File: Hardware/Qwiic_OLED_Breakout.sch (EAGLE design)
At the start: 30 parts, among them J1 QWIIC_RIGHT_ANGLE, J2 QWIIC_RIGHT_ANGLE

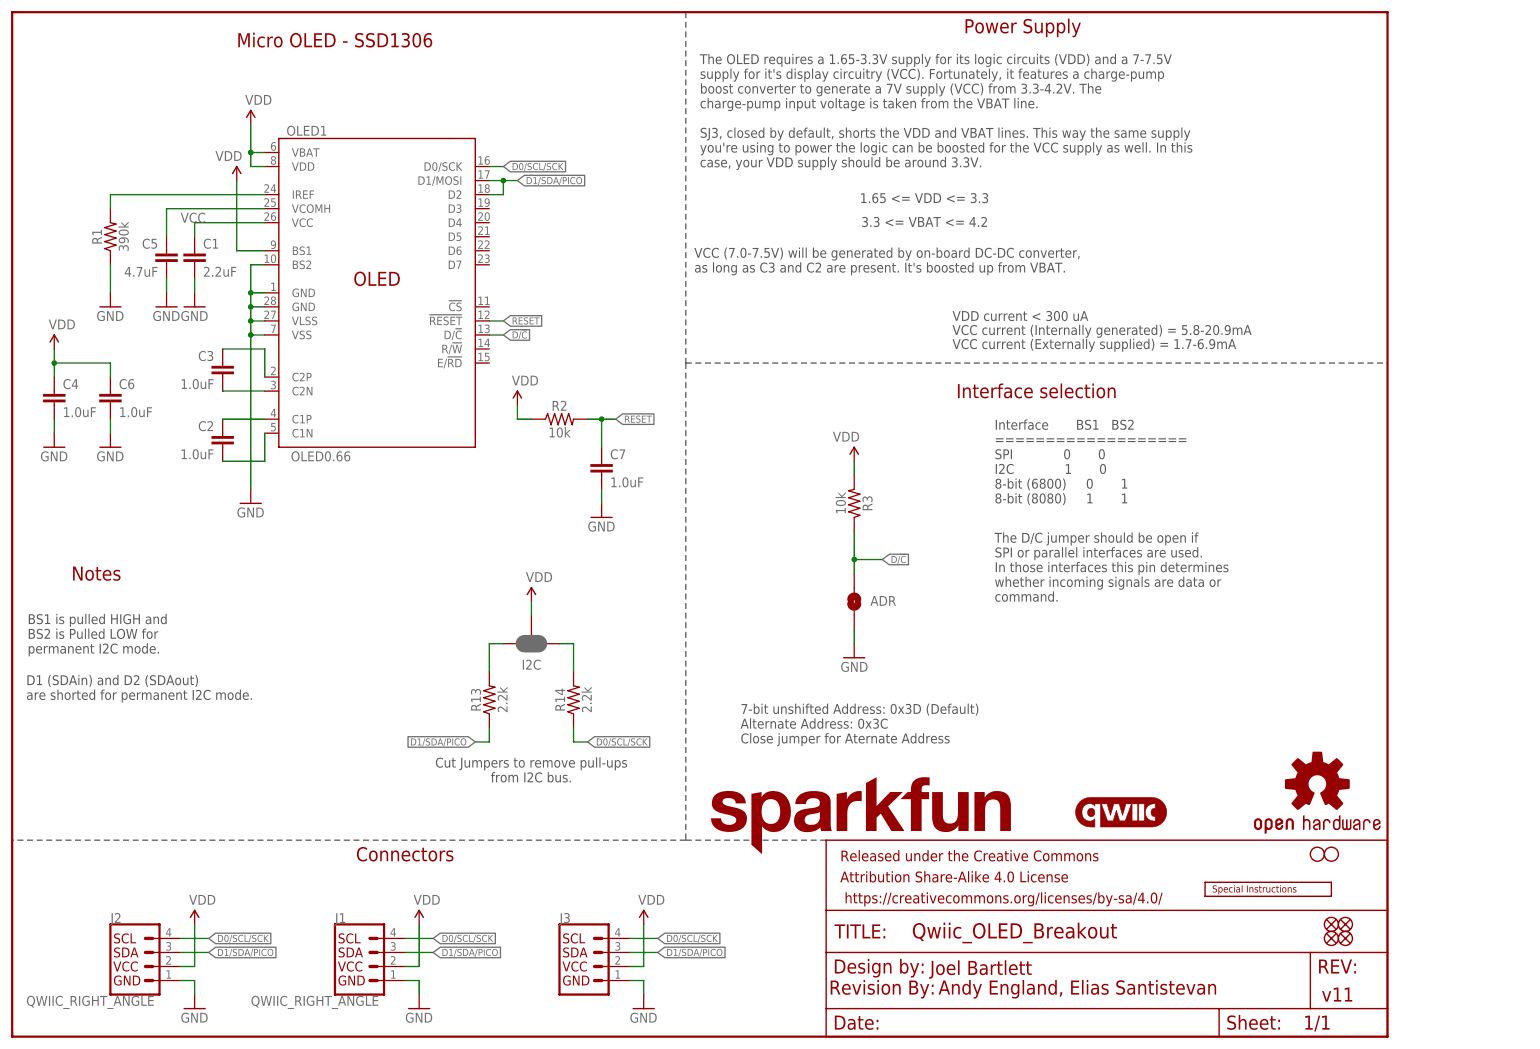
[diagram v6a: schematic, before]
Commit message: Fixes some proportional text, cleans up some nets
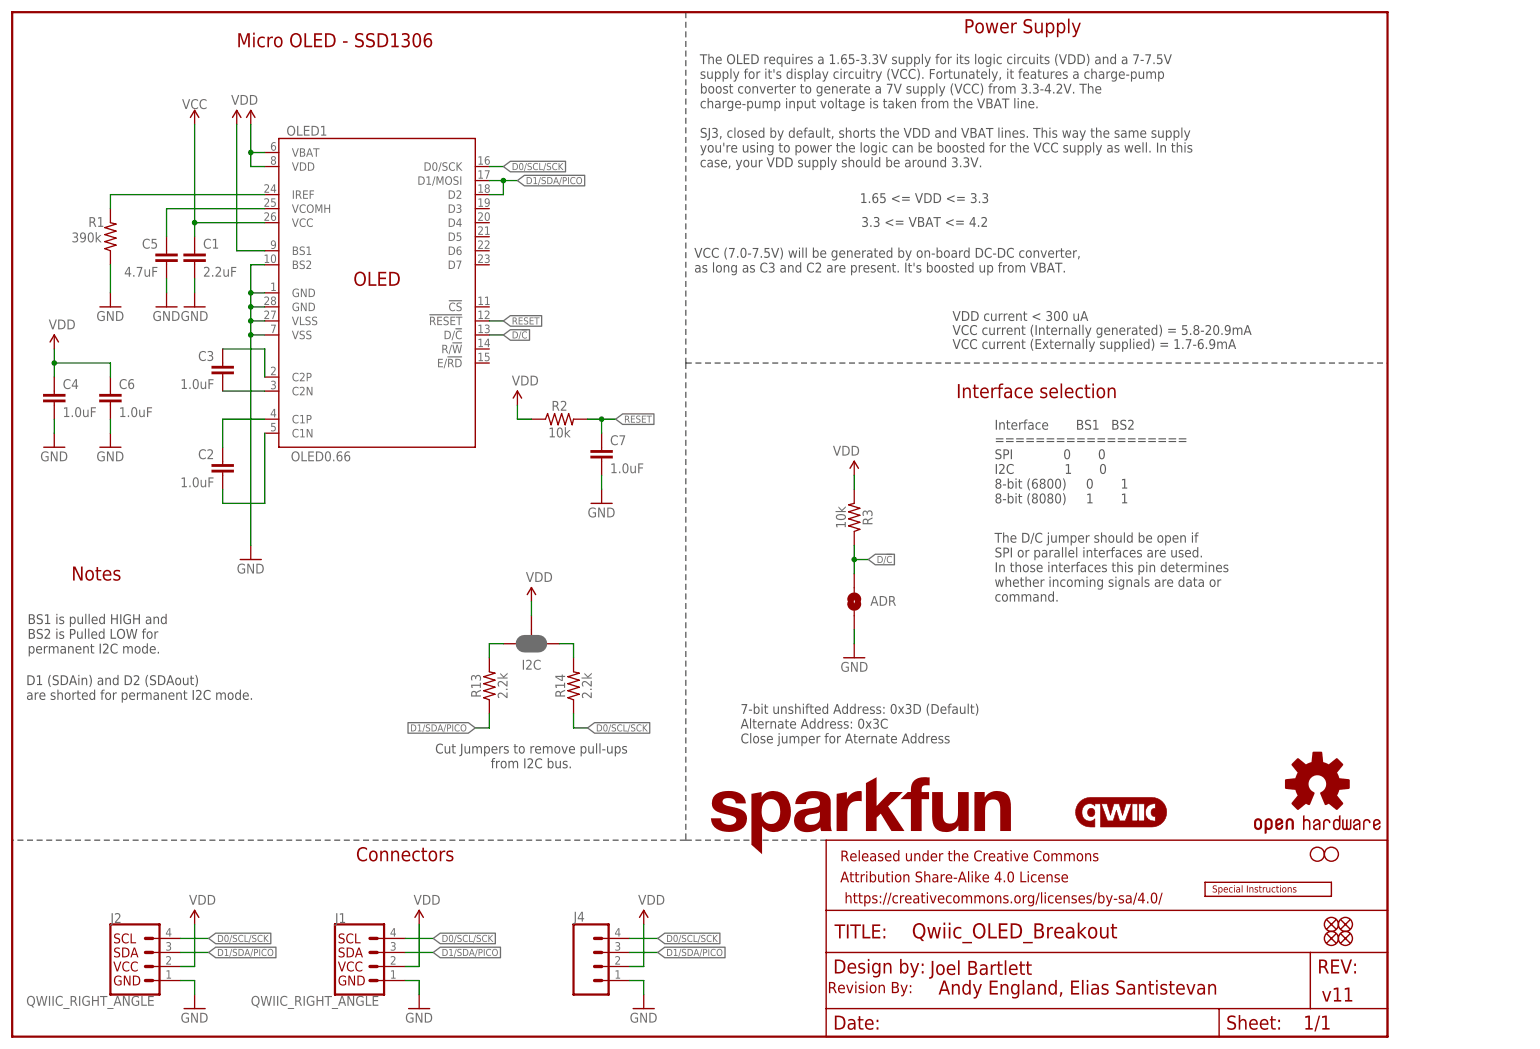
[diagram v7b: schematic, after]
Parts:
- removed J3: (no value), SparkX:I2C_STANDARD_NO_SILK
- removed LOGO1: REVISION, SparkFun-Aesthetics:REVISION
- added J4: (no value), SparkFun-Connectors:CONN_041X04_NO_SILK_NO_POP
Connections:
- net D0/SCL/SCK: now also J4.4; no longer J3.SCL
- net D1/SDA/PICO: now also J4.3; no longer J3.SDA
- net GND: now also J4.1; no longer J3.GND
- net VDD: now also J4.2; no longer J3.VCC
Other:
- note added: "Revision By:"
- moved on the sheet: C2, C7, R13, R14, R3
